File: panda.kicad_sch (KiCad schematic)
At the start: 14 parts

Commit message: clean up repo
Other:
- sheet ADC1: file ADCCircuitry.kicad_sch -> adc_circuitry.kicad_sch
- sheet ADC2: file ADCCircuitry.kicad_sch -> adc_circuitry.kicad_sch
- sheet ADC3: file ThermocoupleADC.kicad_sch -> thermocouple_adc.kicad_sch
- sheet ADC4: file IgnitorADC.kicad_sch -> ignitor_adc.kicad_sch
- sheet ADC5: file ThermocoupleADC.kicad_sch -> thermocouple_adc.kicad_sch
- sheet ESP32 Breakout: file ESP32Breakout.kicad_sch -> esp32_breakout.kicad_sch
- sheet Ignitor Control: file Ignitor_Control.kicad_sch -> ignitor_control.kicad_sch
- sheet Load Cell Measurement: file LoadCellMeasurement.kicad_sch -> load_cell_measurement.kicad_sch
- sheet Power Regulation: file PowerRegulation.kicad_sch -> power_regulation.kicad_sch
- sheet Pressure Transducer Measurement: file PressureTransducerMeasurement.kicad_sch -> pressure_transducer_measurement.kicad_sch
- sheet Thermocouple Measurement: file ThermocoupleMeasurement.kicad_sch -> thermocouple_measurement.kicad_sch
- sheet Valve Control: file ValveControl.kicad_sch -> valve_control.kicad_sch

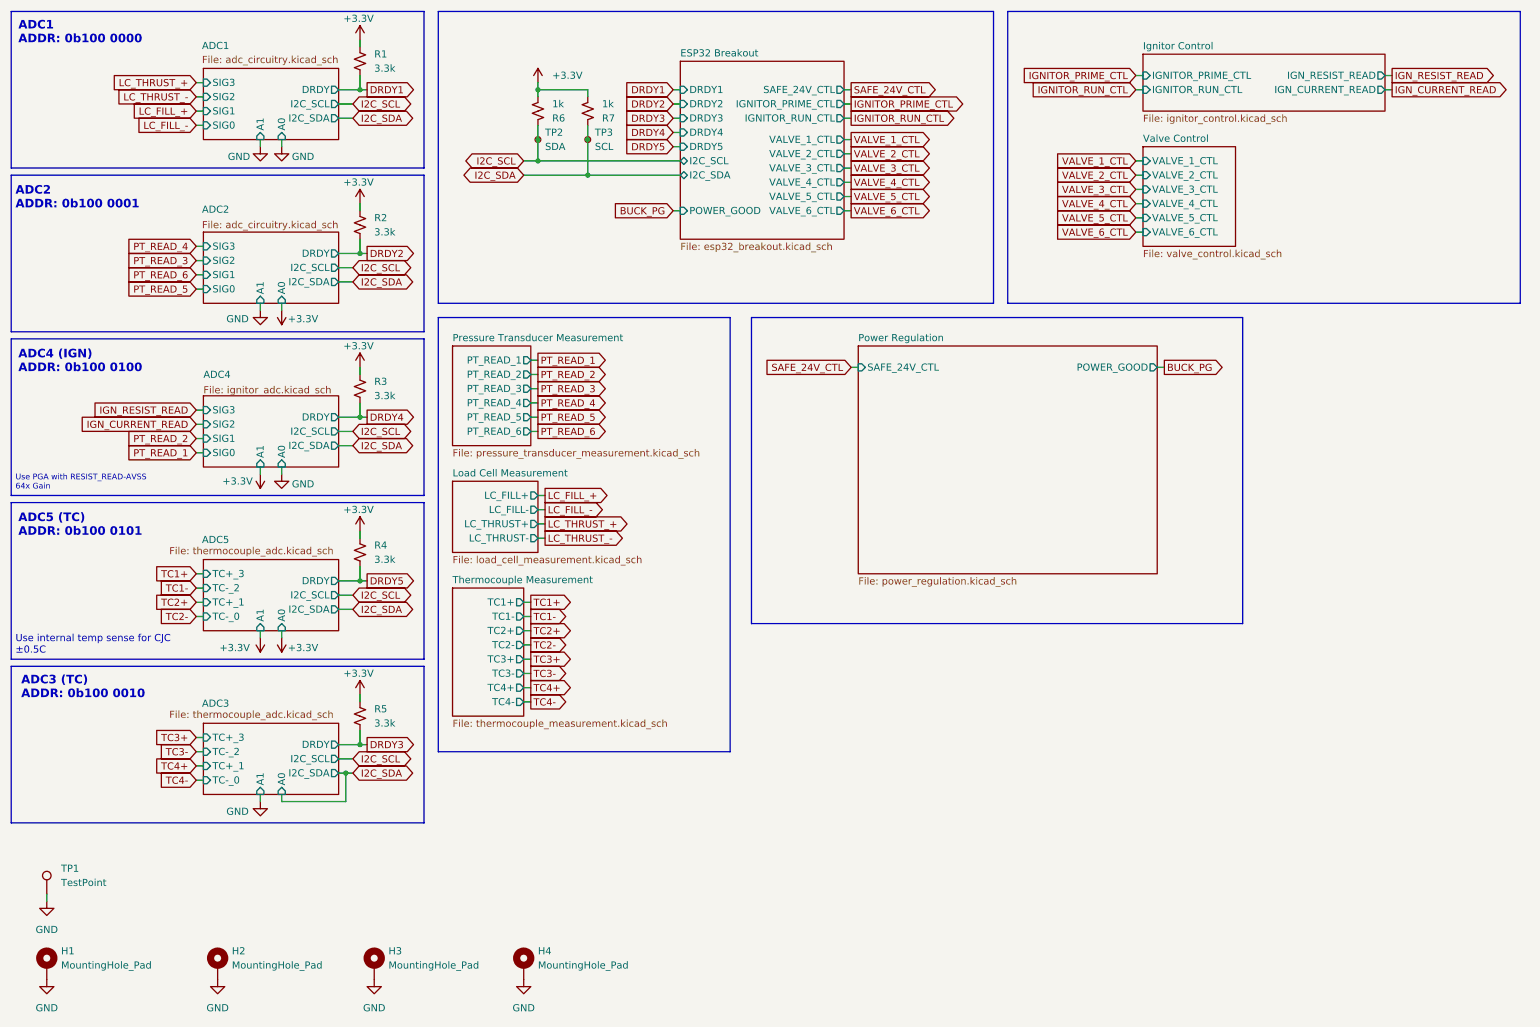
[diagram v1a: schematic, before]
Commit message: remove remainder of leftofer schematics
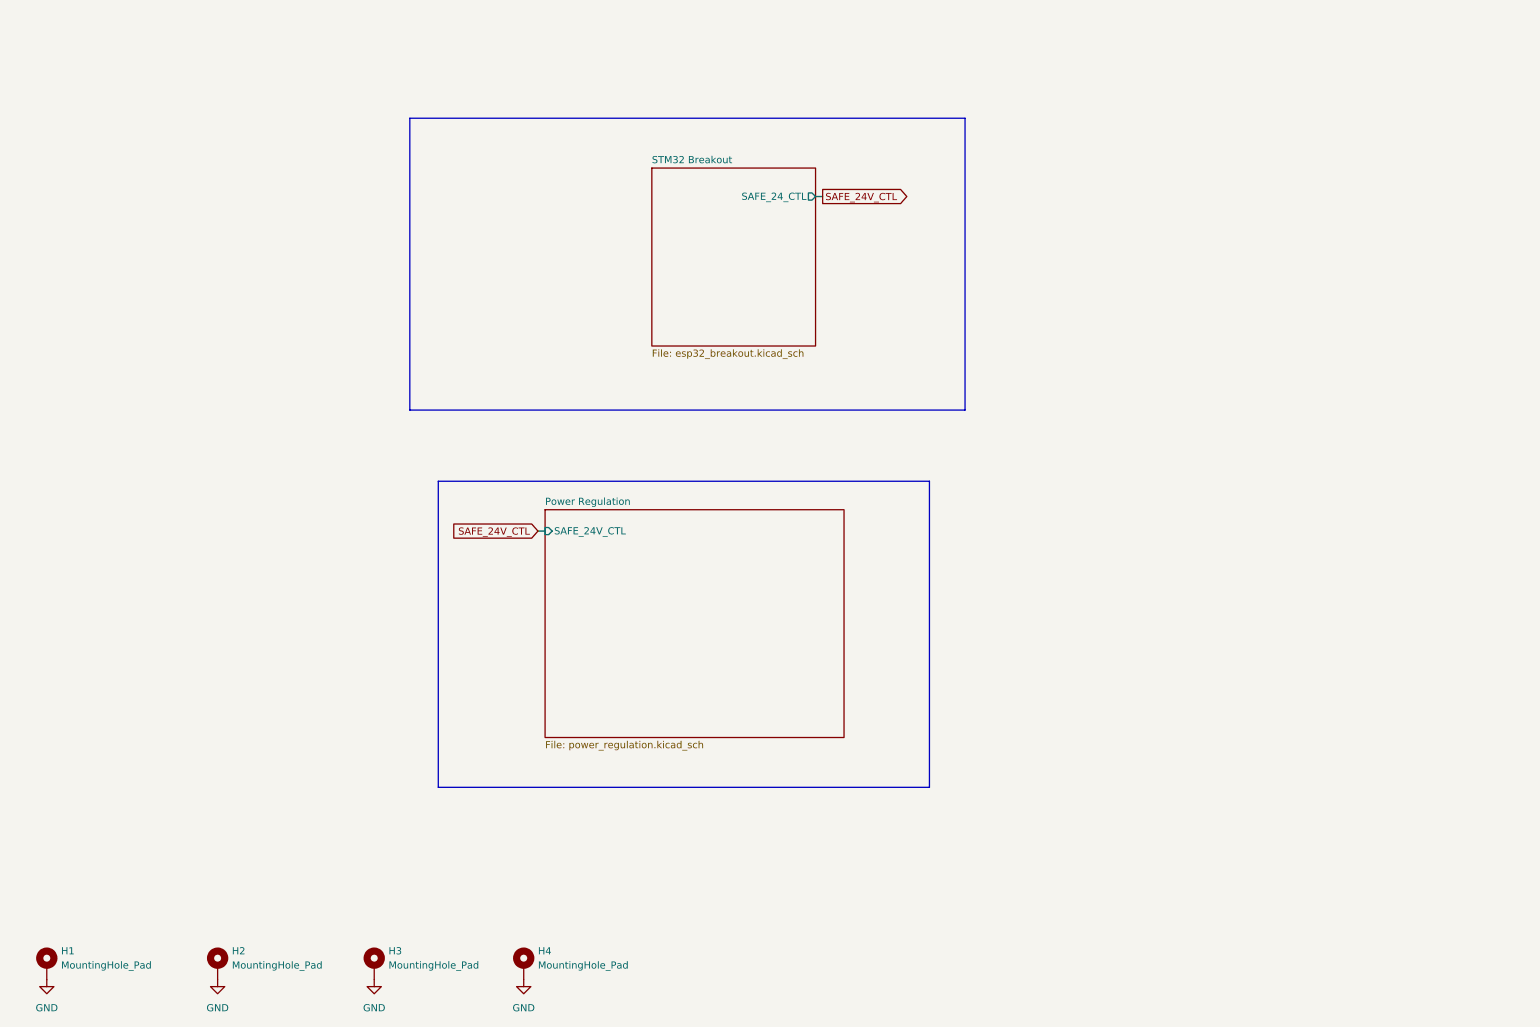
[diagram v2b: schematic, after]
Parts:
- removed R1, R2, R3, R4, R5: 3.3k, Resistor_SMD:R_0402_1005Metric, symbol Device:R_Small_US
- removed R6, R7: 1k, Resistor_SMD:R_0402_1005Metric, symbol Device:R_Small_US
- removed TP1: TestPoint, TestPoint:TestPoint_Loop_D2.50mm_Drill1.0mm, symbol Connector:TestPoint
- removed TP2: SDA, TestPoint:TestPoint_Pad_D1.5mm, symbol Connector:TestPoint_Small
- removed TP3: SCL, TestPoint:TestPoint_Pad_D1.5mm, symbol Connector:TestPoint_Small
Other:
- sheet ESP32 Breakout renamed STM32 Breakout
- removed sheet ADC1
- removed sheet ADC2
- removed sheet ADC3
- removed sheet ADC4
- removed sheet ADC5
- removed sheet Ignitor Control
- removed sheet Load Cell Measurement
- removed sheet Pressure Transducer Measurement
- removed sheet Thermocouple Measurement
- removed sheet Valve Control
- sheet Power Regulation ports: added none; removed POWER_GOOD
- sheet STM32 Breakout ports: added SAFE_24_CTL; removed DRDY1, DRDY2, DRDY3, DRDY4, DRDY5, I2C_SCL, I2C_SDA, IGNITOR_PRIME_CTL, IGNITOR_RUN_CTL, POWER_GOOD, SAFE_24V_CTL, VALVE_1_CTL, VALVE_2_CTL, VALVE_3_CTL, VALVE_4_CTL, VALVE_5_CTL, VALVE_6_CTL
- note removed: "ADC1 ADDR: 0b100 0000"
- note removed: "ADC2 ADDR: 0b100 0001"
- note removed: "ADC3 (TC) ADDR: 0b100 0010"
- note removed: "ADC4 (IGN) ADDR: 0b100 0100"
- note removed: "ADC5 (TC) ADDR: 0b100 0101"
- note removed: "Use PGA with RESIST_READ-AVSS 64x Gain"
- note removed: "Use internal temp sense for CJC ±0.5C"

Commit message: add afe for pressure transducers
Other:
- added sheet Pressure Transducer ADC (pt_adc.kicad_sch)
- sheet STM32 Breakout: file esp32_breakout.kicad_sch -> stm32_breakout.kicad_sch
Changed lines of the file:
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@@
 	)
 	(rectangle
-		(start 90.17 97.79)
-		(end 177.8 152.4)
+		(start 157.48 92.71)
+		(end 245.11 147.32)
 		(stroke
 			(width 0)
@@
 	)
 	(rectangle
-		(start 85.09 33.02)
-		(end 184.15 85.09)
+		(start 152.4 27.94)
+		(end 251.46 80.01)
 		(stroke
 			(width 0)
@@
 	(wire
 		(pts
-			(xy 157.48 46.99) (xy 158.75 46.99)
+			(xy 224.79 41.91) (xy 226.06 41.91)
 		)
 		(stroke
@@
 	(wire
 		(pts
-			(xy 107.95 106.68) (xy 109.22 106.68)
+			(xy 175.26 101.6) (xy 176.53 101.6)
 		)
 		(stroke
@@
 	(global_label "SAFE_24V_CTL"
 		(shape input)
-		(at 107.95 106.68 180)
+		(at 175.26 101.6 180)
 		(fields_autoplaced yes)
 		(effects
@@
 		)
 		(property "Intersheetrefs" "${INTERSHEET_REFS}"
-			(at 91.7206 106.68 0)
+			(at 159.0306 101.6 0)
 			(hide yes)
 			(show_name no)
@@
 	(global_label "SAFE_24V_CTL"
 		(shape output)
-		(at 158.75 46.99 0)
+		(at 226.06 41.91 0)
 		(fields_autoplaced yes)
 		(effects
@@
 		)
 		(property "Intersheetrefs" "${INTERSHEET_REFS}"
-			(at 174.9794 46.99 0)
+			(at 242.2894 41.91 0)
 			(hide yes)
 			(show_name no)
@@
 		(dnp no)
 		(fields_autoplaced yes)
-		(property "Reference" "#PWR018"
+		(property "Reference" "#PWR03"
 			(at 78.74 193.04 0)
 			(hide yes)
@@
 			(project "panda"
 				(path "/226c5870-4123-4efa-a2b3-b42d02f59bb7"
-					(reference "#PWR018")
+					(reference "#PWR03")
 					(unit 1)
 				)
@@
 		(dnp no)
 		(fields_autoplaced yes)
-		(property "Reference" "#PWR019"
+		(property "Reference" "#PWR04"
 			(at 105.41 193.04 0)
 			(hide yes)
@@
 			(project "panda"
 				(path "/226c5870-4123-4efa-a2b3-b42d02f59bb7"
-					(reference "#PWR019")
+					(reference "#PWR04")
 					(unit 1)
 				)
@@
 		(dnp no)
 		(fields_autoplaced yes)
-		(property "Reference" "#PWR02"
+		(property "Reference" "#PWR01"
 			(at 20.32 193.04 0)
 			(hide yes)
@@
 			(project "panda"
 				(path "/226c5870-4123-4efa-a2b3-b42d02f59bb7"
-					(reference "#PWR02")
+					(reference "#PWR01")
 					(unit 1)
 				)
@@
 		(dnp no)
 		(fields_autoplaced yes)
-		(property "Reference" "#PWR03"
+		(property "Reference" "#PWR02"
 			(at 50.8 193.04 0)
 			(hide yes)
@@
 			(project "panda"
 				(path "/226c5870-4123-4efa-a2b3-b42d02f59bb7"
-					(reference "#PWR03")
+					(reference "#PWR02")
 					(unit 1)
 				)
@@
 	)
 	(sheet
-		(at 109.22 102.87)
+		(at 176.53 97.79)
 		(size 53.34 40.64)
 		(exclude_from_sim no)
@@
 		)
 		(property "Sheetname" "Power Regulation"
-			(at 109.22 102.1584 0)
+			(at 176.53 97.0784 0)
 			(show_name no)
 			(do_not_autoplace no)
@@
 		)
 		(property "Sheetfile" "power_regulation.kicad_sch"
-			(at 109.22 144.0946 0)
+			(at 176.53 139.0146 0)
 			(show_name no)
 			(do_not_autoplace no)
@@
 		)
 		(pin "SAFE_24V_CTL" input
-			(at 109.22 106.68 180)
+			(at 176.53 101.6 180)
 			(effects
 				(font
@@
 	)
 	(sheet
-		(at 128.27 41.91)
-		(size 29.21 31.75)
+		(at 31.75 39.37)
+		(size 36.83 19.05)
 		(exclude_from_sim no)
 		(in_bom yes)
@@
 			(color 0 0 0 0)
 		)
+		(property "Sheetname" "Pressure Transducer ADC"
+			(at 31.75 38.6584 0)
+			(show_name no)
+			(do_not_autoplace no)
+			(effects
+				(font
+					(size 1.27 1.27)
+				)
+				(justify left bottom)
+			)
+		)
+		(property "Sheetfile" "pt_adc.kicad_sch"
+			(at 31.75 59.0046 0)
+			(show_name no)
+			(do_not_autoplace no)
+			(effects
+				(font
+					(size 1.27 1.27)
+				)
+				(justify left top)
+			)
+		)
+		(instances
+			(project "panda"
+				(path "/226c5870-4123-4efa-a2b3-b42d02f59bb7"
+					(page "4")
+				)
+			)
+		)
+	)
+	(sheet
+		(at 195.58 36.83)
+		(size 29.21 31.75)
+		(exclude_from_sim no)
+		(in_bom yes)
+		(on_board yes)
+		(dnp no)
+		(fields_autoplaced yes)
+		(stroke
+			(width 0.1524)
+			(type solid)
+		)
+		(fill
+			(color 0 0 0 0)
+		)
 		(property "Sheetname" "STM32 Breakout"
-			(at 128.27 41.1984 0)
+			(at 195.58 36.1184 0)
 			(show_name no)
 			(do_not_autoplace no)
@@
 			)
 		)
-		(property "Sheetfile" "esp32_breakout.kicad_sch"
-			(at 128.27 74.2446 0)
+		(property "Sheetfile" "stm32_breakout.kicad_sch"
+			(at 195.58 69.1646 0)
 			(show_name no)
 			(do_not_autoplace no)
@@
 		)
 		(pin "SAFE_24_CTL" output
-			(at 157.48 46.99 0)
-			(effects
-				(font
+			(at 224.79 41.91 0)
+			(effects
+				(font
